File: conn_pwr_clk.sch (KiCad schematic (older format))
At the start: 1 part, among them J2 Conn_02x02_Odd_Even

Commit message: way to long since last commit
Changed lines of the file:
@@
 EESchema Schematic File Version 4
-LIBS:program_counter_pcb-cache
 EELAYER 30 0
 EELAYER END
 $Descr A4 11693 8268
 encoding utf-8
-Sheet 2 6
+Sheet 13 13
 Title ""
 Date ""
@@
 AR Path="/5EE56D05/5EEF6F5F" Ref="J2"  Part="1"
 AR Path="/5EF3DDE6/5EEF6F5F" Ref="J2"  Part="1"
-F 0 "J2" H 4400 3092 50  0000 C CNN
+AR Path="/5F1B37D5/5EEF6F5F" Ref="J3"  Part="1"
+AR Path="/5F1824C2/5EEF6F5F" Ref="J2"  Part="1"
+AR Path="/5F645C7E/5EEF6F5F" Ref="J5"  Part="1"
+F 0 "J5" H 4400 3092 50  0000 C CNN
 F 1 "Conn_02x02_Odd_Even" H 4400 3001 50  0000 C CNN
 F 2 "Connector_PinHeader_2.54mm:PinHeader_2x02_P2.54mm_Vertical" H 4350 2875 50  0001 C CNN
@@
 AR Path="/5EE56D05/5EEF6F65" Ref="#PWR013"  Part="1"
 AR Path="/5EF3DDE6/5EEF6F65" Ref="#PWR01"  Part="1"
-F 0 "#PWR01" H 3725 2725 50  0001 C CNN
+AR Path="/5F1B37D5/5EEF6F65" Ref="#PWR017"  Part="1"
+AR Path="/5F1824C2/5EEF6F65" Ref="#PWR01"  Part="1"
+AR Path="/5F645C7E/5EEF6F65" Ref="#PWR0133"  Part="1"
+F 0 "#PWR0133" H 3725 2725 50  0001 C CNN
 F 1 "VCC" V 3743 3002 50  0000 L CNN
 F 2 "" H 3725 2875 50  0001 C CNN
@@
 AR Path="/5EE56D05/5EEF6F6B" Ref="#PWR014"  Part="1"
 AR Path="/5EF3DDE6/5EEF6F6B" Ref="#PWR02"  Part="1"
-F 0 "#PWR02" H 5000 2625 50  0001 C CNN
+AR Path="/5F1B37D5/5EEF6F6B" Ref="#PWR018"  Part="1"
+AR Path="/5F1824C2/5EEF6F6B" Ref="#PWR02"  Part="1"
+AR Path="/5F645C7E/5EEF6F6B" Ref="#PWR0134"  Part="1"
+F 0 "#PWR0134" H 5000 2625 50  0001 C CNN
 F 1 "GND" V 5005 2747 50  0000 R CNN
 F 2 "" H 5000 2875 50  0001 C CNN
@@
 AR Path="/5EE56D05/5EEF6F77" Ref="#FLG02"  Part="1"
 AR Path="/5EF3DDE6/5EEF6F77" Ref="#FLG02"  Part="1"
-F 0 "#FLG02" H 5000 2850 50  0001 C CNN
+AR Path="/5F1B37D5/5EEF6F77" Ref="#FLG02"  Part="1"
+AR Path="/5F1824C2/5EEF6F77" Ref="#FLG02"  Part="1"
+AR Path="/5F645C7E/5EEF6F77" Ref="#FLG0101"  Part="1"
+F 0 "#FLG0101" H 5000 2850 50  0001 C CNN
 F 1 "PWR_FLAG" H 5000 2948 50  0000 C CNN
 F 2 "" H 5000 2775 50  0001 C CNN
@@
 AR Path="/5EE56D05/5EEF6F71" Ref="#FLG01"  Part="1"
 AR Path="/5EF3DDE6/5EEF6F71" Ref="#FLG01"  Part="1"
-F 0 "#FLG01" H 3725 2850 50  0001 C CNN
+AR Path="/5F1B37D5/5EEF6F71" Ref="#FLG01"  Part="1"
+AR Path="/5F1824C2/5EEF6F71" Ref="#FLG01"  Part="1"
+AR Path="/5F645C7E/5EEF6F71" Ref="#FLG0102"  Part="1"
+F 0 "#FLG0102" H 3725 2850 50  0001 C CNN
 F 1 "PWR_FLAG" H 3725 2948 50  0000 C CNN
 F 2 "" H 3725 2775 50  0001 C CNN

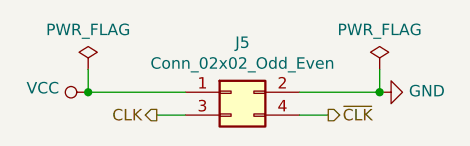
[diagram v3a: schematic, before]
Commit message: add bit operations
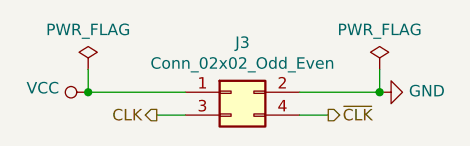
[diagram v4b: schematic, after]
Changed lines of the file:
@@
 EESchema Schematic File Version 4
+LIBS:buttons_pcb-cache
 EELAYER 30 0
 EELAYER END
 $Descr A4 11693 8268
 encoding utf-8
-Sheet 13 13
+Sheet 13 5
 Title ""
 Date ""
@@
 AR Path="/5F1824C2/5EEF6F5F" Ref="J2"  Part="1"
 AR Path="/5F645C7E/5EEF6F5F" Ref="J5"  Part="1"
-F 0 "J5" H 4400 3092 50  0000 C CNN
+AR Path="/5F408F25/5EEF6F5F" Ref="J3"  Part="1"
+F 0 "J3" H 4400 3092 50  0000 C CNN
 F 1 "Conn_02x02_Odd_Even" H 4400 3001 50  0000 C CNN
 F 2 "Connector_PinHeader_2.54mm:PinHeader_2x02_P2.54mm_Vertical" H 4350 2875 50  0001 C CNN
@@
 AR Path="/5F1824C2/5EEF6F65" Ref="#PWR01"  Part="1"
 AR Path="/5F645C7E/5EEF6F65" Ref="#PWR0133"  Part="1"
-F 0 "#PWR0133" H 3725 2725 50  0001 C CNN
+AR Path="/5F408F25/5EEF6F65" Ref="#PWR015"  Part="1"
+F 0 "#PWR015" H 3725 2725 50  0001 C CNN
 F 1 "VCC" V 3743 3002 50  0000 L CNN
 F 2 "" H 3725 2875 50  0001 C CNN
@@
 AR Path="/5F1824C2/5EEF6F6B" Ref="#PWR02"  Part="1"
 AR Path="/5F645C7E/5EEF6F6B" Ref="#PWR0134"  Part="1"
-F 0 "#PWR0134" H 5000 2625 50  0001 C CNN
+AR Path="/5F408F25/5EEF6F6B" Ref="#PWR016"  Part="1"
+F 0 "#PWR016" H 5000 2625 50  0001 C CNN
 F 1 "GND" V 5005 2747 50  0000 R CNN
 F 2 "" H 5000 2875 50  0001 C CNN
@@
 AR Path="/5F1824C2/5EEF6F77" Ref="#FLG02"  Part="1"
 AR Path="/5F645C7E/5EEF6F77" Ref="#FLG0101"  Part="1"
-F 0 "#FLG0101" H 5000 2850 50  0001 C CNN
+AR Path="/5F408F25/5EEF6F77" Ref="#FLG02"  Part="1"
+F 0 "#FLG02" H 5000 2850 50  0001 C CNN
 F 1 "PWR_FLAG" H 5000 2948 50  0000 C CNN
 F 2 "" H 5000 2775 50  0001 C CNN
@@
 AR Path="/5F1824C2/5EEF6F71" Ref="#FLG01"  Part="1"
 AR Path="/5F645C7E/5EEF6F71" Ref="#FLG0102"  Part="1"
-F 0 "#FLG0102" H 3725 2850 50  0001 C CNN
+AR Path="/5F408F25/5EEF6F71" Ref="#FLG01"  Part="1"
+F 0 "#FLG01" H 3725 2850 50  0001 C CNN
 F 1 "PWR_FLAG" H 3725 2948 50  0000 C CNN
 F 2 "" H 3725 2775 50  0001 C CNN

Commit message: memory programmer and cu
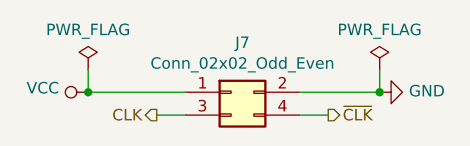
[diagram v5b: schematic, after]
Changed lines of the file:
@@
 EESchema Schematic File Version 4
-LIBS:buttons_pcb-cache
+LIBS:control_unit_pcb-cache
 EELAYER 30 0
 EELAYER END
 $Descr A4 11693 8268
 encoding utf-8
-Sheet 13 5
+Sheet 8 10
 Title ""
 Date ""
@@
 AR Path="/5F645C7E/5EEF6F5F" Ref="J5"  Part="1"
 AR Path="/5F408F25/5EEF6F5F" Ref="J3"  Part="1"
-F 0 "J3" H 4400 3092 50  0000 C CNN
+AR Path="/5F531986/5EEF6F5F" Ref="J7"  Part="1"
+F 0 "J7" H 4400 3092 50  0000 C CNN
 F 1 "Conn_02x02_Odd_Even" H 4400 3001 50  0000 C CNN
 F 2 "Connector_PinHeader_2.54mm:PinHeader_2x02_P2.54mm_Vertical" H 4350 2875 50  0001 C CNN
@@
 AR Path="/5F645C7E/5EEF6F65" Ref="#PWR0133"  Part="1"
 AR Path="/5F408F25/5EEF6F65" Ref="#PWR015"  Part="1"
-F 0 "#PWR015" H 3725 2725 50  0001 C CNN
+AR Path="/5F531986/5EEF6F65" Ref="#PWR0143"  Part="1"
+F 0 "#PWR0143" H 3725 2725 50  0001 C CNN
 F 1 "VCC" V 3743 3002 50  0000 L CNN
 F 2 "" H 3725 2875 50  0001 C CNN
@@
 AR Path="/5F645C7E/5EEF6F6B" Ref="#PWR0134"  Part="1"
 AR Path="/5F408F25/5EEF6F6B" Ref="#PWR016"  Part="1"
-F 0 "#PWR016" H 5000 2625 50  0001 C CNN
+AR Path="/5F531986/5EEF6F6B" Ref="#PWR0144"  Part="1"
+F 0 "#PWR0144" H 5000 2625 50  0001 C CNN
 F 1 "GND" V 5005 2747 50  0000 R CNN
 F 2 "" H 5000 2875 50  0001 C CNN
@@
 AR Path="/5F645C7E/5EEF6F77" Ref="#FLG0101"  Part="1"
 AR Path="/5F408F25/5EEF6F77" Ref="#FLG02"  Part="1"
-F 0 "#FLG02" H 5000 2850 50  0001 C CNN
+AR Path="/5F531986/5EEF6F77" Ref="#FLG0101"  Part="1"
+F 0 "#FLG0101" H 5000 2850 50  0001 C CNN
 F 1 "PWR_FLAG" H 5000 2948 50  0000 C CNN
 F 2 "" H 5000 2775 50  0001 C CNN
@@
 AR Path="/5F645C7E/5EEF6F71" Ref="#FLG0102"  Part="1"
 AR Path="/5F408F25/5EEF6F71" Ref="#FLG01"  Part="1"
-F 0 "#FLG01" H 3725 2850 50  0001 C CNN
+AR Path="/5F531986/5EEF6F71" Ref="#FLG0102"  Part="1"
+F 0 "#FLG0102" H 3725 2850 50  0001 C CNN
 F 1 "PWR_FLAG" H 3725 2948 50  0000 C CNN
 F 2 "" H 3725 2775 50  0001 C CNN

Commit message: connect cu and start creating material csv
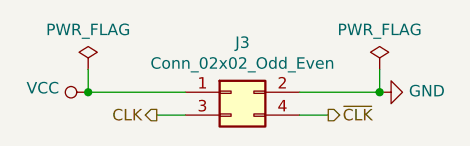
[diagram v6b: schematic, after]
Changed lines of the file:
@@
 EESchema Schematic File Version 4
-LIBS:control_unit_pcb-cache
+LIBS:bit_shifter_pcb-cache
 EELAYER 30 0
 EELAYER END
 $Descr A4 11693 8268
 encoding utf-8
-Sheet 8 10
+Sheet 8 6
 Title ""
 Date ""
@@
 AR Path="/5F408F25/5EEF6F5F" Ref="J3"  Part="1"
 AR Path="/5F531986/5EEF6F5F" Ref="J7"  Part="1"
-F 0 "J7" H 4400 3092 50  0000 C CNN
+F 0 "J3" H 4400 3092 50  0000 C CNN
 F 1 "Conn_02x02_Odd_Even" H 4400 3001 50  0000 C CNN
 F 2 "Connector_PinHeader_2.54mm:PinHeader_2x02_P2.54mm_Vertical" H 4350 2875 50  0001 C CNN
@@
 AR Path="/5F408F25/5EEF6F65" Ref="#PWR015"  Part="1"
 AR Path="/5F531986/5EEF6F65" Ref="#PWR0143"  Part="1"
-F 0 "#PWR0143" H 3725 2725 50  0001 C CNN
+F 0 "#PWR015" H 3725 2725 50  0001 C CNN
 F 1 "VCC" V 3743 3002 50  0000 L CNN
 F 2 "" H 3725 2875 50  0001 C CNN
@@
 AR Path="/5F408F25/5EEF6F6B" Ref="#PWR016"  Part="1"
 AR Path="/5F531986/5EEF6F6B" Ref="#PWR0144"  Part="1"
-F 0 "#PWR0144" H 5000 2625 50  0001 C CNN
+F 0 "#PWR016" H 5000 2625 50  0001 C CNN
 F 1 "GND" V 5005 2747 50  0000 R CNN
 F 2 "" H 5000 2875 50  0001 C CNN
@@
 AR Path="/5F408F25/5EEF6F77" Ref="#FLG02"  Part="1"
 AR Path="/5F531986/5EEF6F77" Ref="#FLG0101"  Part="1"
-F 0 "#FLG0101" H 5000 2850 50  0001 C CNN
+F 0 "#FLG02" H 5000 2850 50  0001 C CNN
 F 1 "PWR_FLAG" H 5000 2948 50  0000 C CNN
 F 2 "" H 5000 2775 50  0001 C CNN
@@
 AR Path="/5F408F25/5EEF6F71" Ref="#FLG01"  Part="1"
 AR Path="/5F531986/5EEF6F71" Ref="#FLG0102"  Part="1"
-F 0 "#FLG0102" H 3725 2850 50  0001 C CNN
+F 0 "#FLG01" H 3725 2850 50  0001 C CNN
 F 1 "PWR_FLAG" H 3725 2948 50  0000 C CNN
 F 2 "" H 3725 2775 50  0001 C CNN

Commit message: part lists
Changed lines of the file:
@@
 EESchema Schematic File Version 4
-LIBS:bit_shifter_pcb-cache
+LIBS:program_counter_pcb-cache
 EELAYER 30 0
 EELAYER END
@@
 AR Path="/5F408F25/5EEF6F5F" Ref="J3"  Part="1"
 AR Path="/5F531986/5EEF6F5F" Ref="J7"  Part="1"
-F 0 "J3" H 4400 3092 50  0000 C CNN
+F 0 "J2" H 4400 3092 50  0000 C CNN
 F 1 "Conn_02x02_Odd_Even" H 4400 3001 50  0000 C CNN
 F 2 "Connector_PinHeader_2.54mm:PinHeader_2x02_P2.54mm_Vertical" H 4350 2875 50  0001 C CNN
@@
 AR Path="/5F408F25/5EEF6F65" Ref="#PWR015"  Part="1"
 AR Path="/5F531986/5EEF6F65" Ref="#PWR0143"  Part="1"
-F 0 "#PWR015" H 3725 2725 50  0001 C CNN
+F 0 "#PWR01" H 3725 2725 50  0001 C CNN
 F 1 "VCC" V 3743 3002 50  0000 L CNN
 F 2 "" H 3725 2875 50  0001 C CNN
@@
 AR Path="/5F408F25/5EEF6F6B" Ref="#PWR016"  Part="1"
 AR Path="/5F531986/5EEF6F6B" Ref="#PWR0144"  Part="1"
-F 0 "#PWR016" H 5000 2625 50  0001 C CNN
+F 0 "#PWR02" H 5000 2625 50  0001 C CNN
 F 1 "GND" V 5005 2747 50  0000 R CNN
 F 2 "" H 5000 2875 50  0001 C CNN
